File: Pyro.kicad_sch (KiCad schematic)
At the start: 37 parts, among them IC5 TPS259830ONRGER, J12 Conn_01x02_Male, Q2 BUK9M11-40EX, U10 SiC437BED-T1-GE3, U9 859-LTV-247

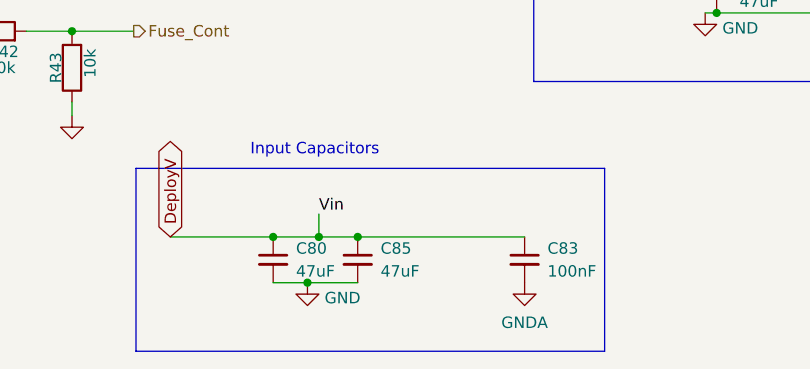
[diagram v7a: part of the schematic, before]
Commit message: added 30V input caps
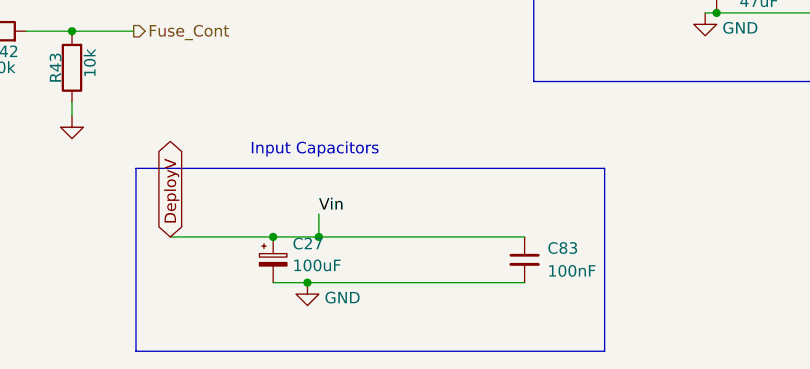
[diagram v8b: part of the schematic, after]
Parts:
- removed C80, C85: 47uF, Capacitor_SMD:C_1206_3216Metric, symbol Device:C_Small
- added C27: 100uF, Capacitor_Tantalum_SMD:CP_EIA-7343-40_Kemet-Y, symbol Device:C_Polarized_Small
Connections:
- net DeployV: now also C27.1
- net GND: now also C27.2
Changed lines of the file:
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@@
 	(paper "A4")
 	(junction
-		(at 147.066 160.274)
+		(at 223.774 64.262)
 		(diameter 0)
 		(color 0 0 0 0)
 	)
 	(junction
-		(at 223.774 64.262)
+		(at 137.668 160.274)
 		(diameter 0)
 		(color 0 0 0 0)
@@
 	)
 	(junction
-		(at 141.478 165.354)
-		(diameter 0)
-		(color 0 0 0 0)
-	)
-	(junction
 		(at 58.674 107.696)
 		(diameter 0)
@@
 	)
 	(junction
+		(at 141.478 165.354)
+		(diameter 0)
+		(color 0 0 0 0)
+	)
+	(junction
 		(at 104.394 121.412)
 		(diameter 0)
@@
 	)
 	(junction
-		(at 137.668 160.274)
-		(diameter 0)
-		(color 0 0 0 0)
-	)
-	(junction
 		(at 49.276 118.872)
 		(diameter 0)
@@
 		)
 	)
-	(polyline
+	(wire
 		(pts
-			(xy 174.498 152.654) (xy 174.498 172.974)
+			(xy 137.668 160.274) (xy 142.748 160.274)
 		)
 		(stroke
@@
 		)
 	)
-	(wire
+	(polyline
 		(pts
-			(xy 174.244 83.312) (xy 174.244 85.852)
+			(xy 174.498 152.654) (xy 174.498 172.974)
 		)
 		(stroke
@@
 	(wire
 		(pts
-			(xy 52.578 63.246) (xy 52.578 68.326)
+			(xy 174.244 83.312) (xy 174.244 85.852)
 		)
 		(stroke
@@
 	(wire
 		(pts
-			(xy 185.674 135.382) (xy 186.944 135.382)
+			(xy 52.578 63.246) (xy 52.578 68.326)
 		)
 		(stroke
@@
 	(wire
 		(pts
-			(xy 141.478 165.354) (xy 147.066 165.354)
+			(xy 185.674 135.382) (xy 186.944 135.382)
 		)
 		(stroke
@@
 		)
 	)
-	(wire
-		(pts
-			(xy 126.238 160.274) (xy 137.668 160.274)
-		)
-		(stroke
-			(width 0)
-			(type default)
-		)
-	)
 	(polyline
 		(pts
@@
 	(wire
 		(pts
-			(xy 137.668 160.274) (xy 142.748 160.274)
+			(xy 126.238 160.274) (xy 137.668 160.274)
 		)
 		(stroke
@@
 	(wire
 		(pts
+			(xy 141.478 165.354) (xy 165.608 165.354)
+		)
+		(stroke
+			(width 0)
+			(type default)
+		)
+	)
+	(wire
+		(pts
 			(xy 110.998 73.406) (xy 110.998 78.486)
 		)
@@
 	(wire
 		(pts
-			(xy 142.748 160.274) (xy 147.066 160.274)
+			(xy 142.748 160.274) (xy 165.608 160.274)
 		)
 		(stroke
@@
 	(wire
 		(pts
-			(xy 147.066 160.274) (xy 165.608 160.274)
-		)
-		(stroke
-			(width 0)
-			(type default)
-		)
-	)
-	(wire
-		(pts
 			(xy 61.214 98.552) (xy 61.214 101.092)
 		)
@@
 	)
 	(symbol
-		(lib_id "Device:LED")
-		(at 103.378 67.056 90)
+		(lib_id "Device:C_Polarized_Small")
+		(at 137.668 162.814 0)
 		(unit 1)
 		(exclude_from_sim no)
@@
 		(dnp no)
 		(fields_autoplaced yes)
-		(property "Reference" "D4"
-			(at 107.188 68.0085 90)
+		(property "Reference" "C27"
+			(at 139.827 161.0557 0)
 			(effects
 				(font
 					(size 1.27 1.27)
 				)
-				(justify right)
+				(justify left)
 			)
 		)
-		(property "Value" "RED_LED"
-			(at 107.188 70.5485 90)
+		(property "Value" "100uF"
+			(at 139.827 163.48 0)
 			(effects
 				(font
 					(size 1.27 1.27)
 				)
-				(justify right)
+				(justify left)
 			)
 		)
-		(property "Footprint" "LED_SMD:LED_0603_1608Metric"
-			(at 103.378 67.056 0)
+		(property "Footprint" "Capacitor_Tantalum_SMD:CP_EIA-7343-40_Kemet-Y"
+			(at 137.668 162.814 0)
 			(effects
 				(font
@@
 		)
 		(property "Datasheet" "~"
-			(at 103.378 67.056 0)
+			(at 137.668 162.814 0)
 			(effects
 				(font
@@
 		)
 		(property "Description" ""
-			(at 103.378 67.056 0)
+			(at 137.668 162.814 0)
 			(effects
 				(font
@@
 			(project "Ricardo-Stark"
 				(path "/7db990e4-92e1-4f99-b4d2-435bbec1ba83/3c6662b6-8783-49dc-b944-3dc2b3e30a07"
-					(reference "D4")
+					(reference "C27")
 					(unit 1)
 				)
@@
 	)
 	(symbol
-		(lib_id "power:GNDA")
-		(at 165.608 165.354 0)
+		(lib_id "Device:LED")
+		(at 103.378 67.056 90)
 		(unit 1)
 		(exclude_from_sim no)
@@
 		(dnp no)
 		(fields_autoplaced yes)
-		(property "Reference" "#PWR0177"
-			(at 165.608 171.704 0)
+		(property "Reference" "D4"
+			(at 107.188 68.0085 90)
 			(effects
 				(font
 					(size 1.27 1.27)
 				)
-				(hide yes)
+				(justify right)
 			)
 		)
-		(property "Value" "GNDA"
-			(at 165.608 169.7974 0)
+		(property "Value" "RED_LED"
+			(at 107.188 70.5485 90)
 			(effects
 				(font
 					(size 1.27 1.27)
 				)
+				(justify right)
 			)
 		)
-		(property "Footprint" ""
-			(at 165.608 165.354 0)
+		(property "Footprint" "LED_SMD:LED_0603_1608Metric"
+			(at 103.378 67.056 0)
 			(effects
 				(font
@@
 			)
 		)
-		(property "Datasheet" ""
-			(at 165.608 165.354 0)
+		(property "Datasheet" "~"
+			(at 103.378 67.056 0)
 			(effects
 				(font
@@
 		)
 		(property "Description" ""
-			(at 165.608 165.354 0)
+			(at 103.378 67.056 0)
 			(effects
 				(font
@@
 		(pin "1"
 		)
+		(pin "2"
+		)
 		(instances
 			(project "Ricardo-Stark"
 				(path "/7db990e4-92e1-4f99-b4d2-435bbec1ba83/3c6662b6-8783-49dc-b944-3dc2b3e30a07"
-					(reference "#PWR0177")
+					(reference "D4")
 					(unit 1)
 				)
@@
 	)
 	(symbol
-		(lib_id "Device:C_Small")
-		(at 137.668 162.814 0)
-		(unit 1)
-		(exclude_from_sim no)
-		(in_bom yes)
-		(on_board yes)
-		(dnp no)
-		(fields_autoplaced yes)
-		(property "Reference" "C80"
-			(at 140.208 161.5503 0)
-			(effects
-				(font
-					(size 1.27 1.27)
-				)
-				(justify left)
-			)
-		)
-		(property "Value" "47uF"
-			(at 140.208 164.0903 0)
-			(effects
-				(font
-					(size 1.27 1.27)
-				)
-				(justify left)
-			)
-		)
-		(property "Footprint" "Capacitor_SMD:C_1206_3216Metric"
-			(at 137.668 162.814 0)
-			(effects
-				(font
-					(size 1.27 1.27)
-				)
-				(hide yes)
-			)
-		)
-		(property "Datasheet" "~"
-			(at 137.668 162.814 0)
-			(effects
-				(font
-					(size 1.27 1.27)
-				)
-				(hide yes)
-			)
-		)
-		(property "Description" ""
-			(at 137.668 162.814 0)
-			(effects
-				(font
-					(size 1.27 1.27)
-				)
-				(hide yes)
-			)
-		)
-		(pin "1"
-		)
-		(pin "2"
-		)
-		(instances
-			(project "Ricardo-Stark"
-				(path "/7db990e4-92e1-4f99-b4d2-435bbec1ba83/3c6662b6-8783-49dc-b944-3dc2b3e30a07"
-					(reference "C80")
-					(unit 1)
-				)
-			)
-		)
-	)
-	(symbol
 		(lib_id "Device:R")
 		(at 103.378 59.436 0)
@@
 					(unit 1)
 				)
-			)
-		)
-	)
-	(symbol
-		(lib_id "Device:C_Small")
-		(at 147.066 162.814 0)
-		(unit 1)
-		(exclude_from_sim no)
-		(in_bom yes)
-		(on_board yes)
-		(dnp no)
-		(fields_autoplaced yes)
-		(property "Reference" "C85"
-			(at 149.606 161.5503 0)
-			(effects
-				(font
-					(size 1.27 1.27)
-				)
-				(justify left)
-			)
-		)
-		(property "Value" "47uF"
-			(at 149.606 164.0903 0)
-			(effects
-				(font
-					(size 1.27 1.27)
-				)
-				(justify left)
-			)
-		)
-		(property "Footprint" "Capacitor_SMD:C_1206_3216Metric"
-			(at 147.066 162.814 0)
-			(effects
-				(font
-					(size 1.27 1.27)
-				)
-				(hide yes)
-			)
-		)
-		(property "Datasheet" "~"
-			(at 147.066 162.814 0)
-			(effects
-				(font
-					(size 1.27 1.27)
-				)
-				(hide yes)
-			)
-		)
-		(property "Description" ""
-			(at 147.066 162.814 0)
-			(effects
-				(font
-					(size 1.27 1.27)
-				)
-				(hide yes)
-			)
-		)
-		(pin "1"
-		)
-		(pin "2"
-		)
-		(instances
-			(project "Ricardo-Stark"
-				(path "/7db990e4-92e1-4f99-b4d2-435bbec1ba83/3c6662b6-8783-49dc-b944-3dc2b3e30a07"
-					(reference "C85")
-					(unit 1)
-				)
